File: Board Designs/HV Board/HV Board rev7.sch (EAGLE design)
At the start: 58 parts, among them IC1 OKI-78SR, IC2 NE5532SOIC

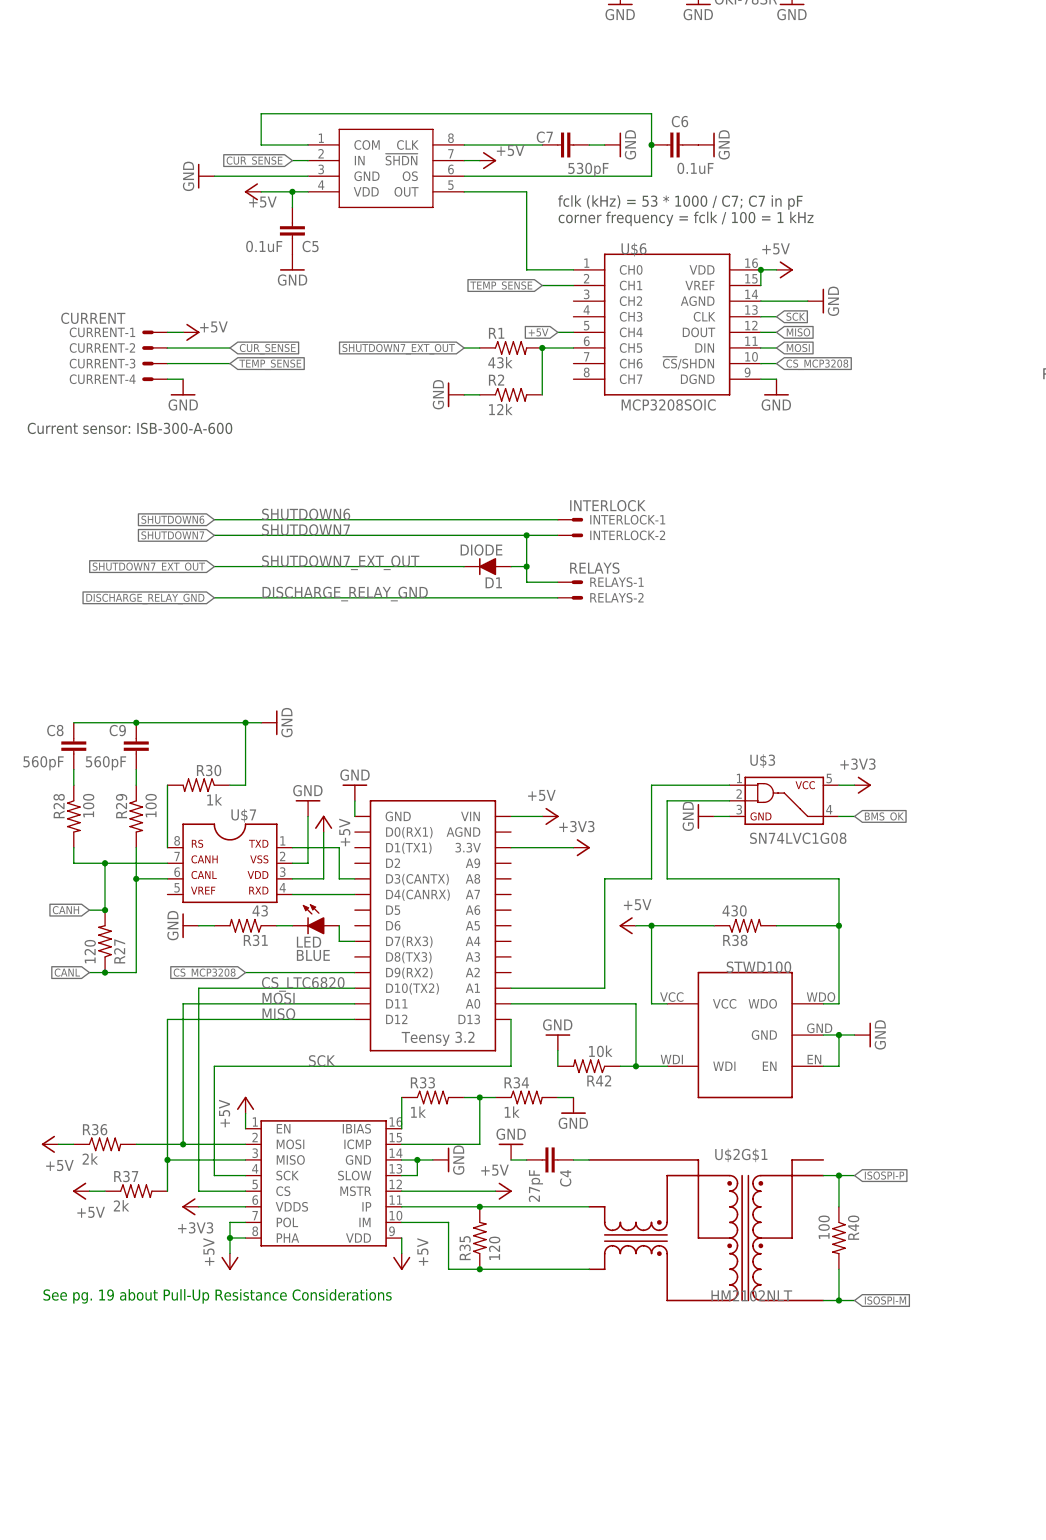
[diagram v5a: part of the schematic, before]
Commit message: HV rev 6&7: added TXB0104 to fix MSP 3208 voltage issue
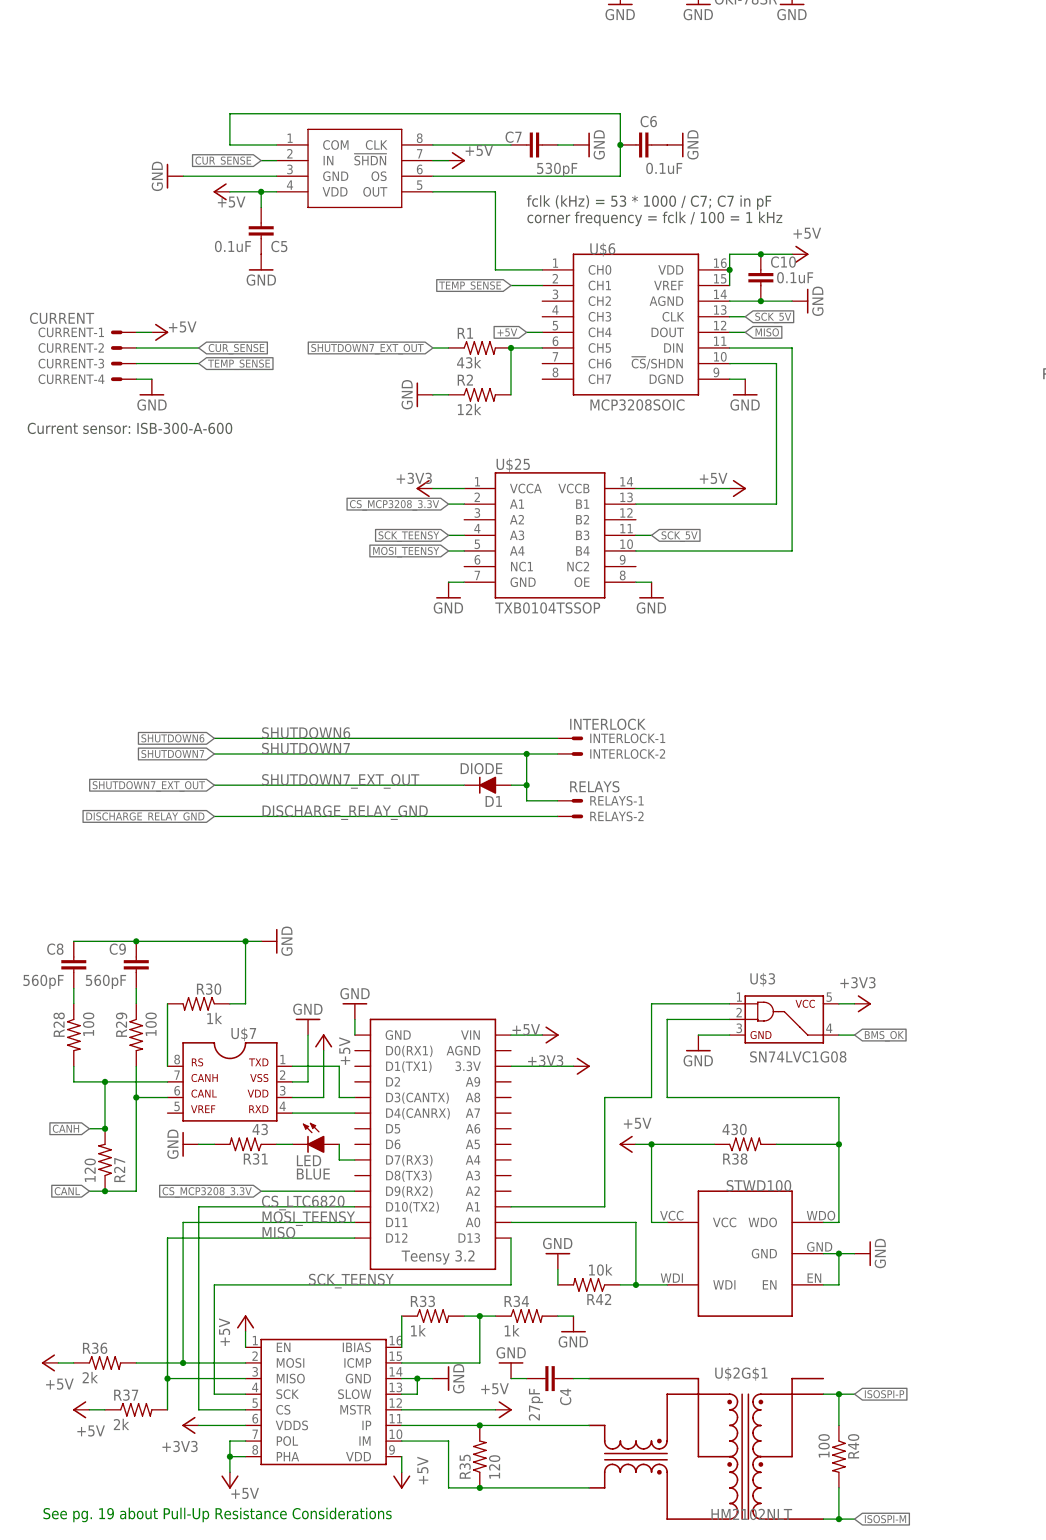
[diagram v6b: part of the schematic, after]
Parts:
- added C10: 0.1uF, HyTechDevices:CAP0805
- added U$25: TXB0104TSSOP, HyTechDevices:TXB0104TSSOP
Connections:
- removed net CS_MCP3208: U$6.!CS!/SHDN, U$9.D9(RX2)
- removed net MOSI: R36.2, U$6.DIN, U$8.MOSI, U$9.D11
- removed net SCK: U$6.CLK, U$8.SCK, U$9.D13
- new net CS_MCP3208_3.3V: U$25.A1, U$9.D9(RX2)
- new net MOSI_5V: U$25.B4, U$6.DIN
- new net MOSI_TEENSY: R36.2, U$25.A4, U$8.MOSI, U$9.D11
- new net N$7: U$25.B1, U$6.!CS!/SHDN
- new net SCK_5V: U$25.B3, U$6.CLK
- new net SCK_TEENSY: U$25.A3, U$8.SCK, U$9.D13
- net +3V3: now also U$25.VCCA
- net +5V: now also C10.1, U$25.VCCB
- net GND: now also C10.2, U$25.GND, U$25.OE
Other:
- moved on the sheet: C4, C5, C6, C7, C8, C9, CURRENT-1, CURRENT-2, CURRENT-3, CURRENT-4, D1, INTERLOCK-1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

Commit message: Move TXB0104 changes to rev 8 & 9
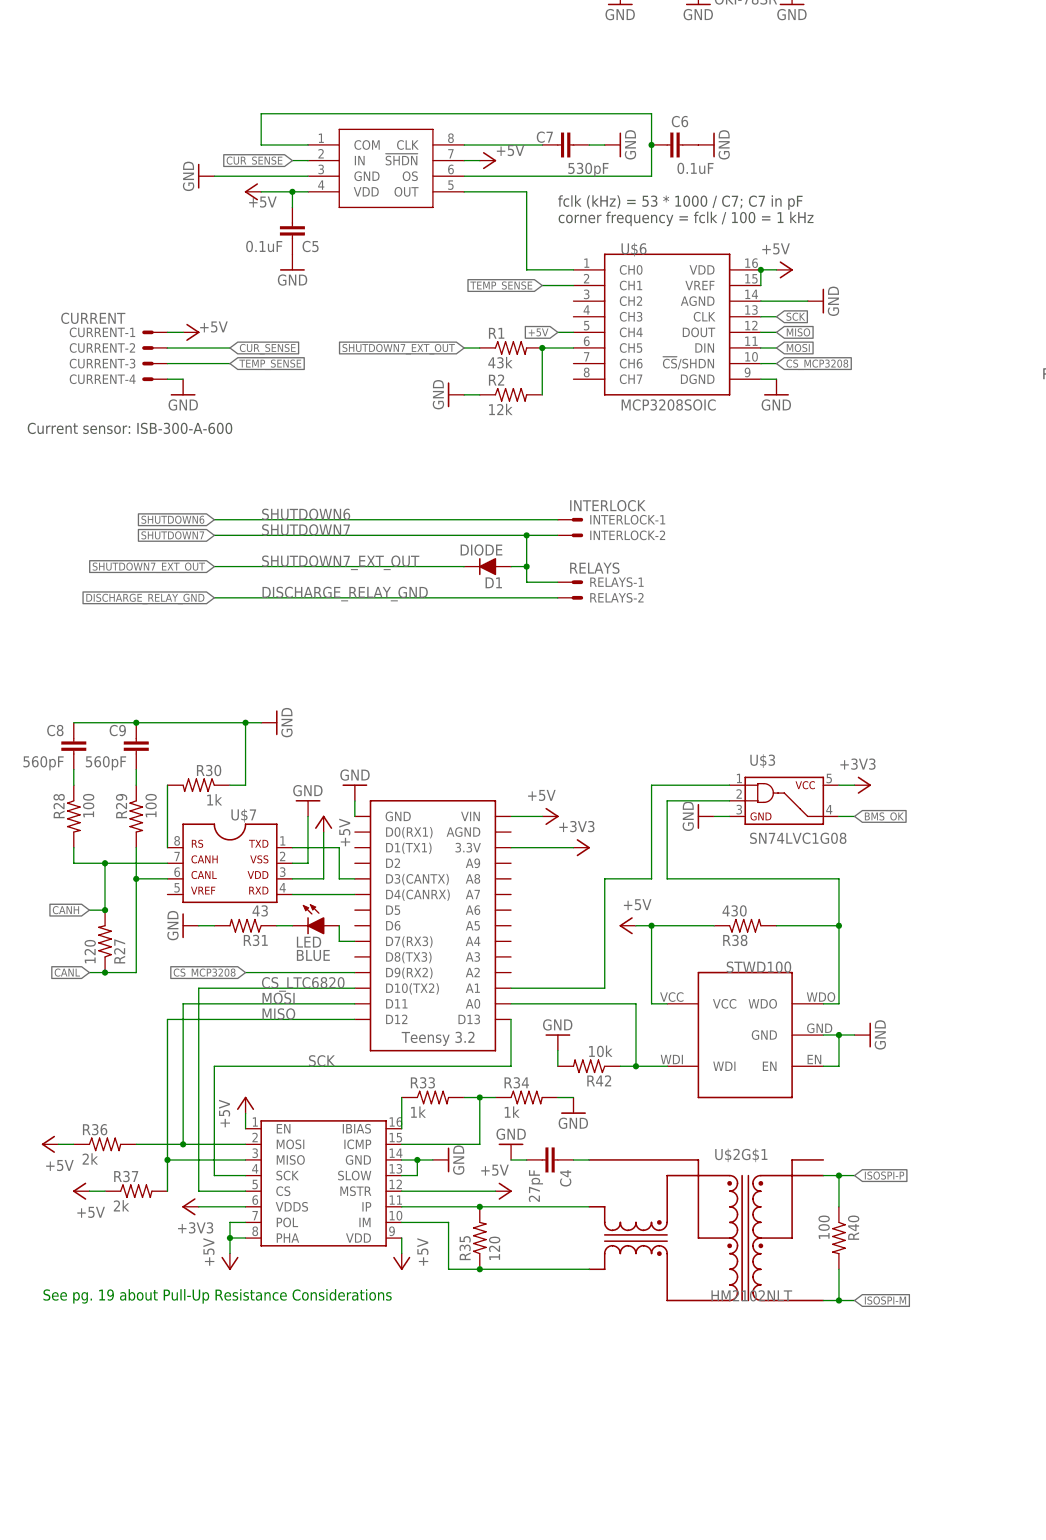
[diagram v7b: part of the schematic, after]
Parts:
- removed C10: 0.1uF, HyTechDevices:CAP0805
- removed U$25: TXB0104TSSOP, HyTechDevices:TXB0104TSSOP
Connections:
- removed net CS_MCP3208_3.3V: U$25.A1, U$9.D9(RX2)
- removed net MOSI_5V: U$25.B4, U$6.DIN
- removed net MOSI_TEENSY: R36.2, U$25.A4, U$8.MOSI, U$9.D11
- removed net N$7: U$25.B1, U$6.!CS!/SHDN
- removed net SCK_5V: U$25.B3, U$6.CLK
- removed net SCK_TEENSY: U$25.A3, U$8.SCK, U$9.D13
- new net CS_MCP3208: U$6.!CS!/SHDN, U$9.D9(RX2)
- new net MOSI: R36.2, U$6.DIN, U$8.MOSI, U$9.D11
- new net SCK: U$6.CLK, U$8.SCK, U$9.D13
- net +3V3: no longer U$25.VCCA
- net +5V: no longer C10.1, U$25.VCCB
- net GND: no longer C10.2, U$25.GND, U$25.OE
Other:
- moved on the sheet: C4, C5, C6, C7, C8, C9, CURRENT-1, CURRENT-2, CURRENT-3, CURRENT-4, D1, INTERLOCK-1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
